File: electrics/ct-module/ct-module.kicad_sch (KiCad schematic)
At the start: 43 parts, among them J1 North, J3 West, J4 East, J5 SJ1-3533NG, J6 SJ1-3533NG, J7 SJ1-3533NG, U1 BA033CC0FP-E2, U2 ADS1115IDGS, U3 MAX3486

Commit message: Review Fixes
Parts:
- removed D4, D8, D9: 3V3, Diode_SMD:D_SOD-523, symbol Device:D_Zener
- C1, C2, C4, C6, C7: manf# C1206C104M6RACTU -> C1206C104M5RACTU; mouser# 80-C1206C104M6R -> 80-C1206C104M5R
- C3, C5, C9: manf# (none) -> C1206C106M9RACTU; mouser# (none) -> 80-C1206C106M9R
- D1: footprint Diode_SMD:D_SOD-523 -> Diode_SMD:D_SOD-123; manf# CPDU24V -> MMSZ5253C-E3-08; mouser# 750-CPDU24V -> 78-MMSZ5253C-E3-08
- D10, D5, D6, D7: value TVS -> 3V3; manf# (none) -> CG0603MLC-3.3LE; mouser# (none) -> 652-CG0603MLC-3.3LE
- D2: footprint Diode_THT:D_DO-41_SOD81_P10.16mm_Horizontal -> Diode_SMD:D_SOD-323_HandSoldering
- D3: value D_TVS -> 3V3
- R10, R11, R12, R14, R5, R6, R7, R8, R9: manf# (none) -> CR1206-JW-103ELF; mouser# (none) -> 652-CR1206JW-103ELF
- U2: footprint Package_SO:TSSOP-10_3x3mm_P0.5mm -> Package_SO:VSSOP-10_3x3mm_P0.5mm

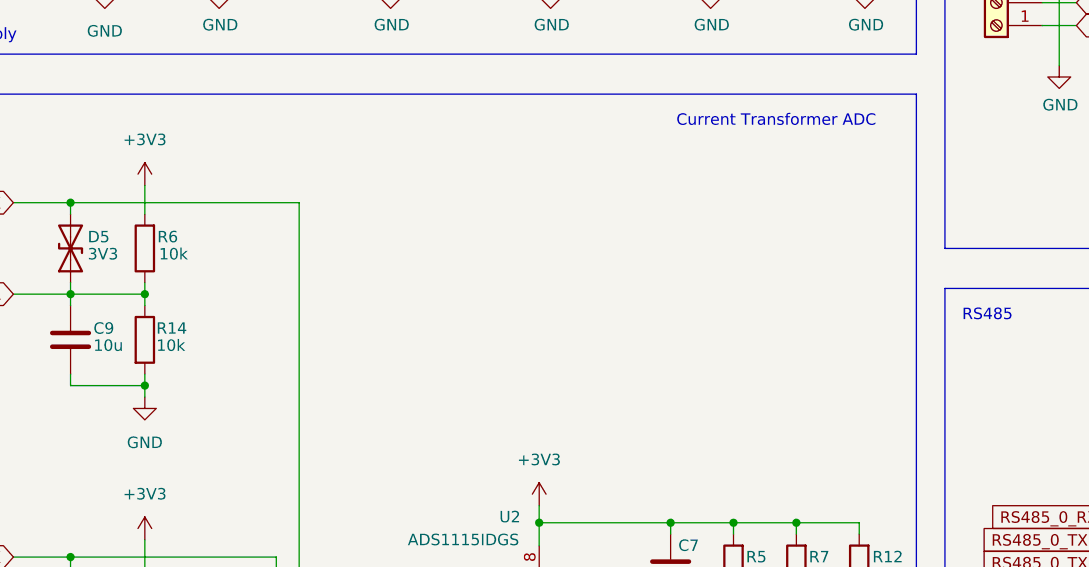
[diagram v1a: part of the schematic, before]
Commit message: INOA-372 Finalize CT module
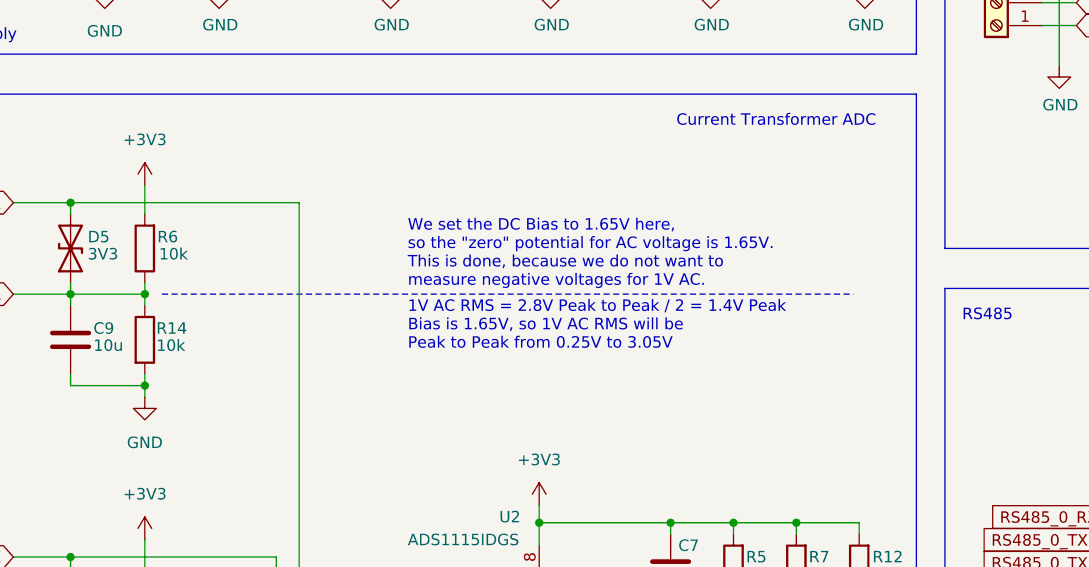
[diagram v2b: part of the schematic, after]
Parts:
- D10, D5, D6, D7: footprint Diode_SMD:D_SOD-523 -> Diode_SMD:D_0603_1608Metric_Pad1.05x0.95mm_HandSolder
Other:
- note added: "1V AC RMS = 2.8V Peak to Peak / 2 = 1.4V Peak Bias is 1.65V, so 1V AC RMS will be Peak to Peak from 0.25V to 3.05V"
- note added: "We set the DC Bias to 1.65V here, so the "zero" potential for AC voltage is 1.65V. This is done, because we do not want to measure negative voltages for 1V AC."
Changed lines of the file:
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@@
     (stroke (width 0) (type default) (color 0 0 0 0))
+  )
+  (polyline (pts (xy 49.53 87.63) (xy 126.365 87.63))
+    (stroke (width 0) (type dot) (color 0 0 0 0))
   )
   (wire (pts (xy 147.32 47.625) (xy 149.225 47.625))
@@
   )
   (text "Bus Mapping" (at 215.265 22.86 0)
+    (effects (font (size 1.27 1.27)) (justify left bottom))
+  )
+  (text "1V AC RMS = 2.8V Peak to Peak / 2 = 1.4V Peak\nBias is 1.65V, so 1V AC RMS will be\nPeak to Peak from 0.25V to 3.05V\n"
+    (at 76.835 93.98 0)
+    (effects (font (size 1.27 1.27)) (justify left bottom))
+  )
+  (text "We set the DC Bias to 1.65V here,\nso the \"zero\" potential for AC voltage is 1.65V.\nThis is done, because we do not want to\nmeasure negative voltages for 1V AC."
+    (at 76.835 86.995 0)
     (effects (font (size 1.27 1.27)) (justify left bottom))
   )
@@
       (effects (font (size 1.27 1.27)) (justify right))
     )
-    (property "Footprint" "Diode_SMD:D_SOD-523" (id 2) (at 39.37 160.655 0)
+    (property "Footprint" "Diode_SMD:D_0603_1608Metric_Pad1.05x0.95mm_HandSolder" (id 2) (at 39.37 160.655 0)
       (effects (font (size 1.27 1.27)) hide)
     )
@@
       (effects (font (size 1.27 1.27)) (justify right))
     )
-    (property "Footprint" "Diode_SMD:D_SOD-523" (id 2) (at 39.37 82.55 0)
+    (property "Footprint" "Diode_SMD:D_0603_1608Metric_Pad1.05x0.95mm_HandSolder" (id 2) (at 39.37 82.55 0)
       (effects (font (size 1.27 1.27)) hide)
     )
@@
       (effects (font (size 1.27 1.27)) (justify right))
     )
-    (property "Footprint" "Diode_SMD:D_SOD-523" (id 2) (at 39.37 121.92 0)
+    (property "Footprint" "Diode_SMD:D_0603_1608Metric_Pad1.05x0.95mm_HandSolder" (id 2) (at 39.37 121.92 0)
       (effects (font (size 1.27 1.27)) hide)
     )
@@
       (effects (font (size 1.27 1.27)) (justify right))
     )
-    (property "Footprint" "Diode_SMD:D_SOD-523" (id 2) (at 76.835 147.32 0)
+    (property "Footprint" "Diode_SMD:D_0603_1608Metric_Pad1.05x0.95mm_HandSolder" (id 2) (at 76.835 147.32 0)
       (effects (font (size 1.27 1.27)) hide)
     )
@@
     )
     (path "/f046ae18-15bf-4972-a4d6-1d4022ceb7ea"
-      (reference "D5") (unit 1) (value "3V3") (footprint "Diode_SMD:D_SOD-523")
+      (reference "D5") (unit 1) (value "3V3") (footprint "Diode_SMD:D_0603_1608Metric_Pad1.05x0.95mm_HandSolder")
     )
     (path "/f0f1405a-aa1b-4b94-97d4-fcd8b73396bb"
-      (reference "D6") (unit 1) (value "3V3") (footprint "Diode_SMD:D_SOD-523")
+      (reference "D6") (unit 1) (value "3V3") (footprint "Diode_SMD:D_0603_1608Metric_Pad1.05x0.95mm_HandSolder")
     )
     (path "/7a8d4c2b-2d3e-4d79-921c-511e245e8dcf"
-      (reference "D7") (unit 1) (value "3V3") (footprint "Diode_SMD:D_SOD-523")
+      (reference "D7") (unit 1) (value "3V3") (footprint "Diode_SMD:D_0603_1608Metric_Pad1.05x0.95mm_HandSolder")
     )
     (path "/f38f5d72-dc27-435f-91d5-011dcbd1b40a"
-      (reference "D10") (unit 1) (value "3V3") (footprint "Diode_SMD:D_SOD-523")
+      (reference "D10") (unit 1) (value "3V3") (footprint "Diode_SMD:D_0603_1608Metric_Pad1.05x0.95mm_HandSolder")
     )
     (path "/11d75bf4-5480-4a2f-baa3-58a51cac0470"
